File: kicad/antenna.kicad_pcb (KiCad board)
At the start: 2 copper layers, 84.1 x 61.7 mm, 44 parts, among them J1 Bus_PCI_Express_x1, J4 Conn_01x02, J6 USB_C_Receptacle_USB2.0_16P, U2 RP2040, U4 W25Q128JVP, U9 MCP25625T-E/ML, X1 ABM8-272-T3, Y2 X322516MLB4SI

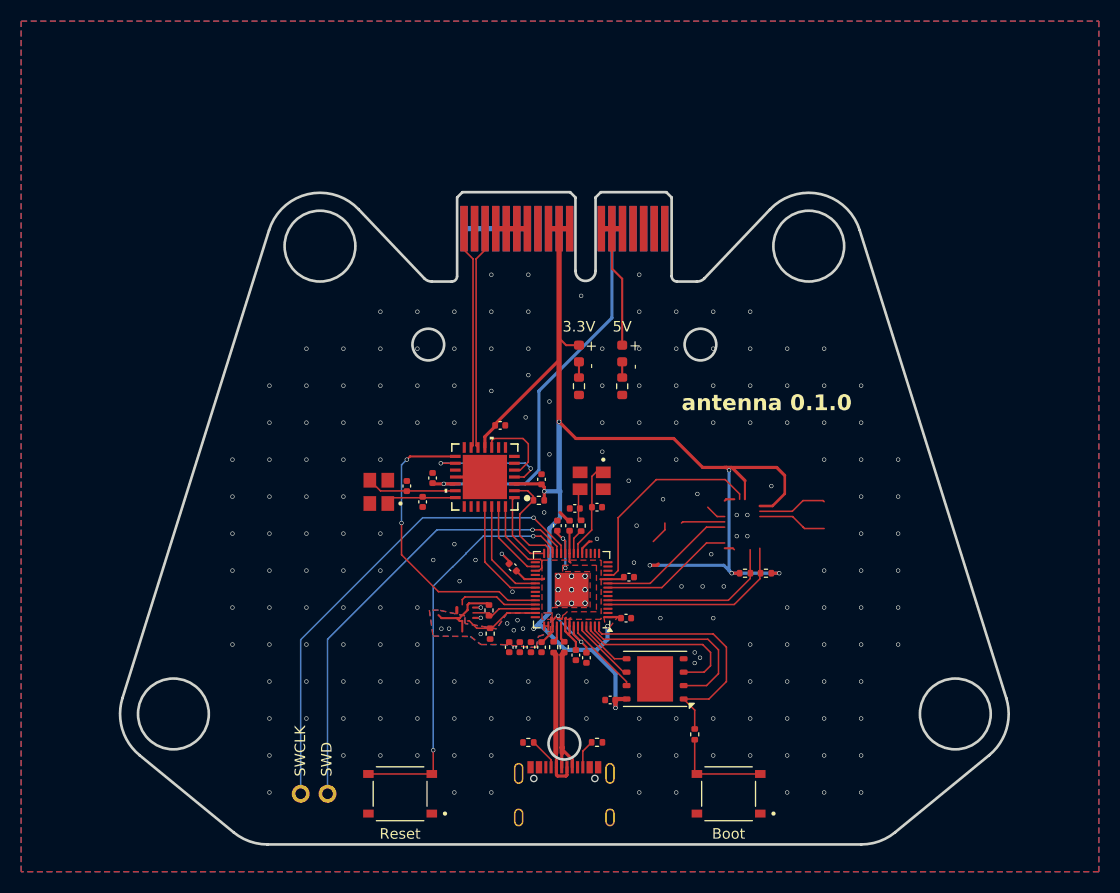
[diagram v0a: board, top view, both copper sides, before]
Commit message: update DXF to new hole positions
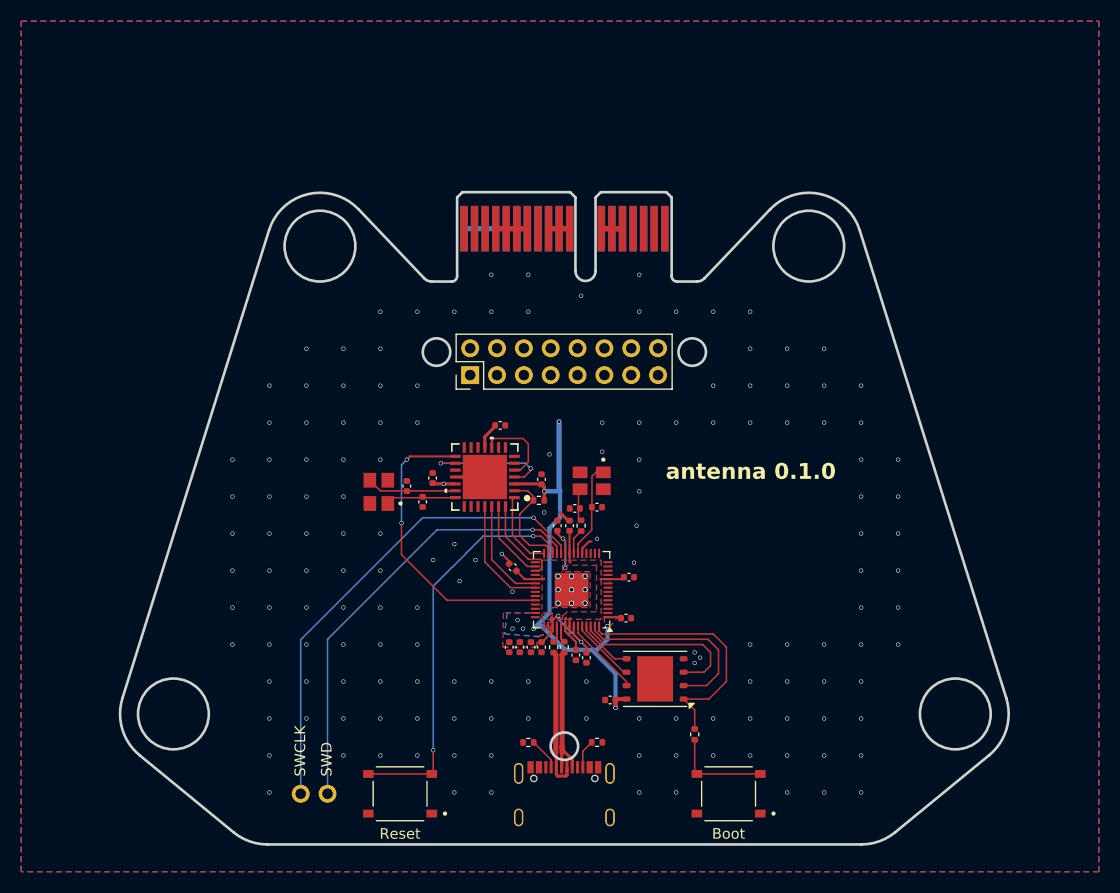
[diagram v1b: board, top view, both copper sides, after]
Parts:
- removed D1, D2: LED, LED_SMD:LED_0603_1608Metric
- removed R1, R2: 150, Resistor_SMD:R_0603_1608Metric
- removed R220, R221, R222, R223: 4.7k, Resistor_SMD:R_0402_1005Metric
- added J5: Conn_02x08_Odd_Even, Connector_PinSocket_2.54mm:PinSocket_2x08_P2.54mm_Vertical, F.Cu at (137.5, 78.0)
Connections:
- U2 pad 11: BOOT_LOAD -> unconnected-(U2-GPIO8-Pad11)
- U2 pad 39: BMPINT -> unconnected-(U2-GPIO27_ADC1-Pad39)
- U2 pad 4: SDA1 -> unconnected-(U2-GPIO2-Pad4)
- U2 pad 40: SDA0 -> unconnected-(U2-GPIO28_ADC2-Pad40)
- U2 pad 41: SCL0 -> unconnected-(U2-GPIO29_ADC3-Pad41)
- U2 pad 5: SCL1 -> unconnected-(U2-GPIO3-Pad5)
- U2 pad 8: BNOINT -> unconnected-(U2-GPIO6-Pad8)
- U2 pad 9: BNORESET -> unconnected-(U2-GPIO7-Pad9)
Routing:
- net +3.3V: track 166.5 -> 65.6 mm, vias 16 -> 8
- net +5V: track 52.6 -> 5.89 mm
- net (no net): track 21.4 -> 0.00 mm
- net CANP: track 21.1 -> 0.00 mm
- net CANN: track 21.1 -> 0.00 mm
- net BOOT_LOAD: track 20.2 -> 0.00 mm
- net SDA1: track 18.3 -> 0.00 mm
- net SCL1: track 17.0 -> 0.00 mm
- net BNORESET: track 13.3 -> 0.00 mm
- net BNOINT: track 12.8 -> 0.00 mm
- net BMPINT: track 7.80 -> 0.00 mm
- net SCL0: track 7.30 -> 0.00 mm
- net SDA0: track 6.29 -> 0.00 mm
- net GND: track 20.2 -> 16.3 mm, vias 201 -> 164
- net Net-(D2-K): track 1.49 -> 0.00 mm
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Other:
- outline, holes or cut-outs redrawn
- board text removed: "3.3V"
- board text removed: "5V"

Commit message: update positioning of all chips to fit rfd900x
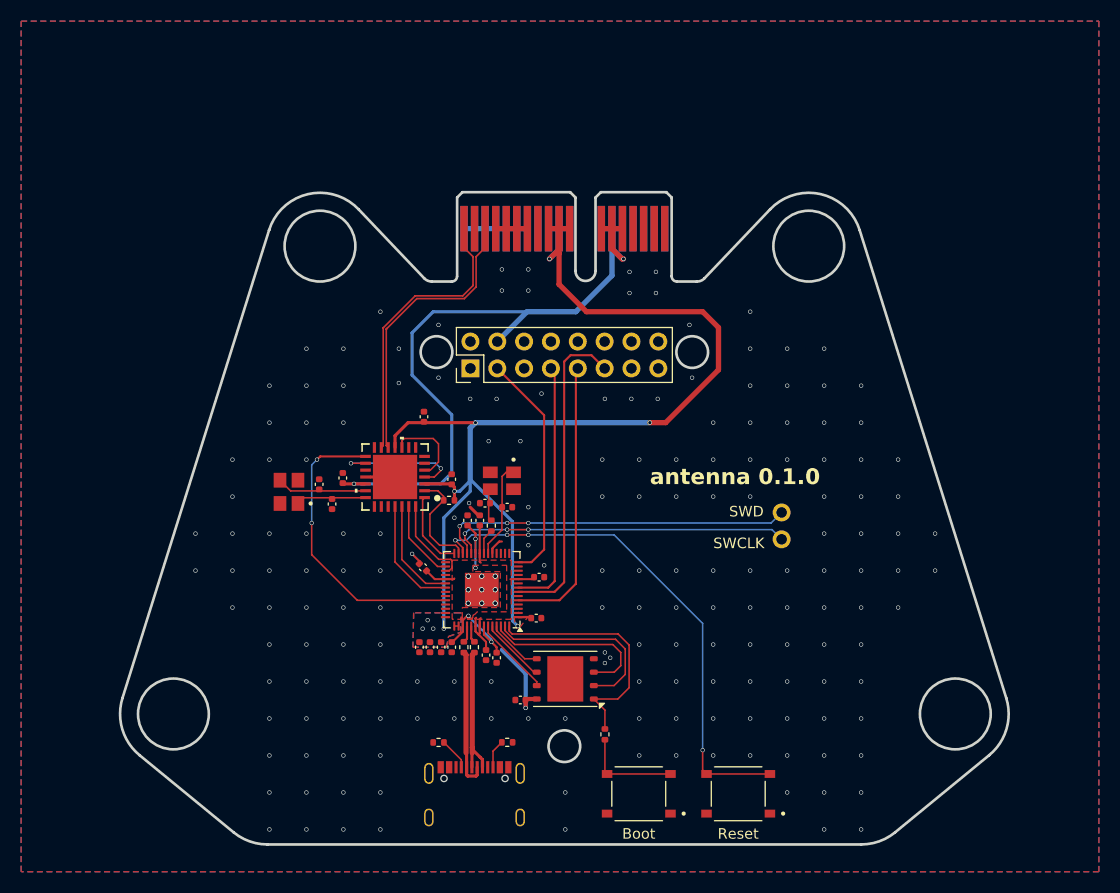
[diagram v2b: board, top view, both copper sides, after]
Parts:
- moved J4 51.5 mm to (167.0, 93.5), turned to 180 degrees
- moved S2 32.0 mm to (162.9, 117.6)
- moved J5 9.11 mm to (146.4, 76.1)
- moved C94 8.58 mm to (124.4, 90.2)
- moved C11 8.51 mm to (138.9, 90.1)
- moved C207 8.51 mm to (137.2, 91.8)
- moved C214 8.51 mm to (138.4, 91.8)
- moved C10 8.50 mm to (141.0, 90.5)
- moved C206 8.50 mm to (140.0, 104.8)
- moved C208 8.50 mm to (135.8, 103.8)
- moved C209 8.50 mm to (139.0, 104.5)
- moved C210 8.50 mm to (134.8, 103.8)
- moved C211 8.50 mm to (143.8, 101.0)
- moved C212 8.50 mm to (133.0, 96.2)
- moved C213 8.50 mm to (144.0, 97.1)
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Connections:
- J5 pad 4: Vcc -> +5V
- U2 pad 14: unconnected-(U2-GPIO11-Pad14) -> CTS
- U2 pad 5: unconnected-(U2-GPIO3-Pad5) -> TX
- U2 pad 7: unconnected-(U2-GPIO5-Pad7) -> RTS
- U2 pad 8: unconnected-(U2-GPIO6-Pad8) -> RX
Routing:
- net +3.3V: track 65.6 -> 137.4 mm, vias 8 -> 10
- net +5V: track 5.89 -> 66.7 mm, vias 1 -> 2
- net RTS: track 0.00 -> 30.6 mm
- net CANN: track 0.00 -> 27.4 mm
- net CANP: track 0.00 -> 27.3 mm
- net TX: track 0.00 -> 26.9 mm
- net RX: track 0.00 -> 24.8 mm
- net CTS: track 0.00 -> 21.9 mm
- net /SWCLK: track 45.9 -> 32.6 mm, vias 1 -> 3
- net /RUN: track 38.0 -> 49.0 mm, vias 2 -> 4
- net /SWD: track 41.8 -> 33.9 mm, vias 1 -> 3
- net /QSPI_SS: track 24.4 -> 23.5 mm
- net /QSPI_SD1: track 18.9 -> 18.3 mm
- net GND: vias 164 -> 190
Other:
- outline, holes or cut-outs redrawn

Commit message: reposition usb ports and buttons
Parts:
- moved R4 11.5 mm to (123.0, 112.8)
- moved J6 10.8 mm to (127.2, 117.6)
- moved R3 10.8 mm to (130.3, 112.8)
- moved S1 6.75 mm to (160.2, 117.6)
- moved S2 6.50 mm to (169.4, 117.6)
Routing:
- net USB_D-: track 13.4 -> 0.00 mm
- net USB_D+: track 13.2 -> 0.00 mm
- net /~{USB_BOOT_S}: track 9.32 -> 0.00 mm
- net /RUN: track 49.0 -> 40.6 mm
- net Net-(J6-CC1): track 3.03 -> 0.00 mm
- net Net-(J6-CC2): track 2.71 -> 0.00 mm
- net GND: vias 190 -> 163
